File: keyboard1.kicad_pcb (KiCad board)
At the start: 2 copper layers, 117.5 x 78.5 mm, 46 parts, among them SW1 SW_PUSH, SW10 SW_PUSH, SW11 SW_PUSH, SW12 SW_PUSH, SW13 SW_PUSH, SW14 SW_PUSH, SW15 SW_PUSH, SW16 SW_PUSH, SW17 SW_PUSH, SW18 SW_PUSH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

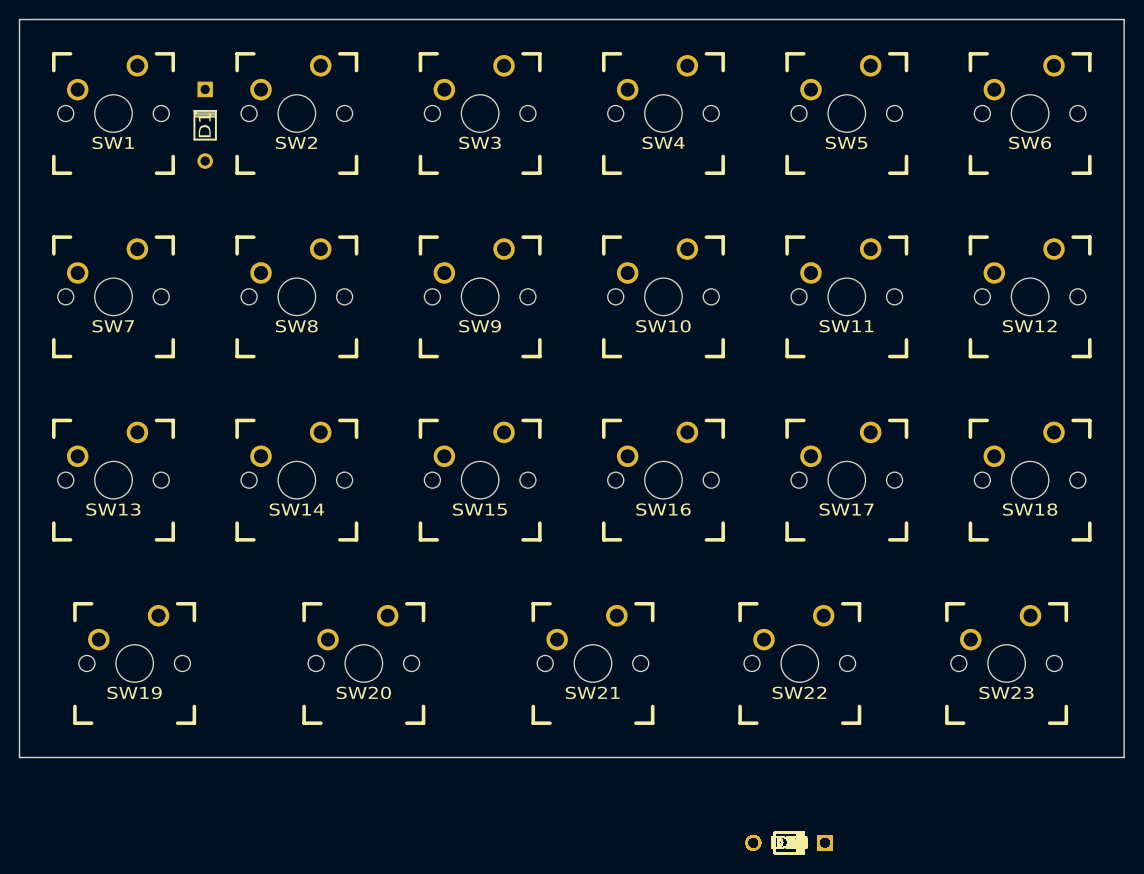
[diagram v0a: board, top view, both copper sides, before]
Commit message: Basic schematic complete, routing in progress
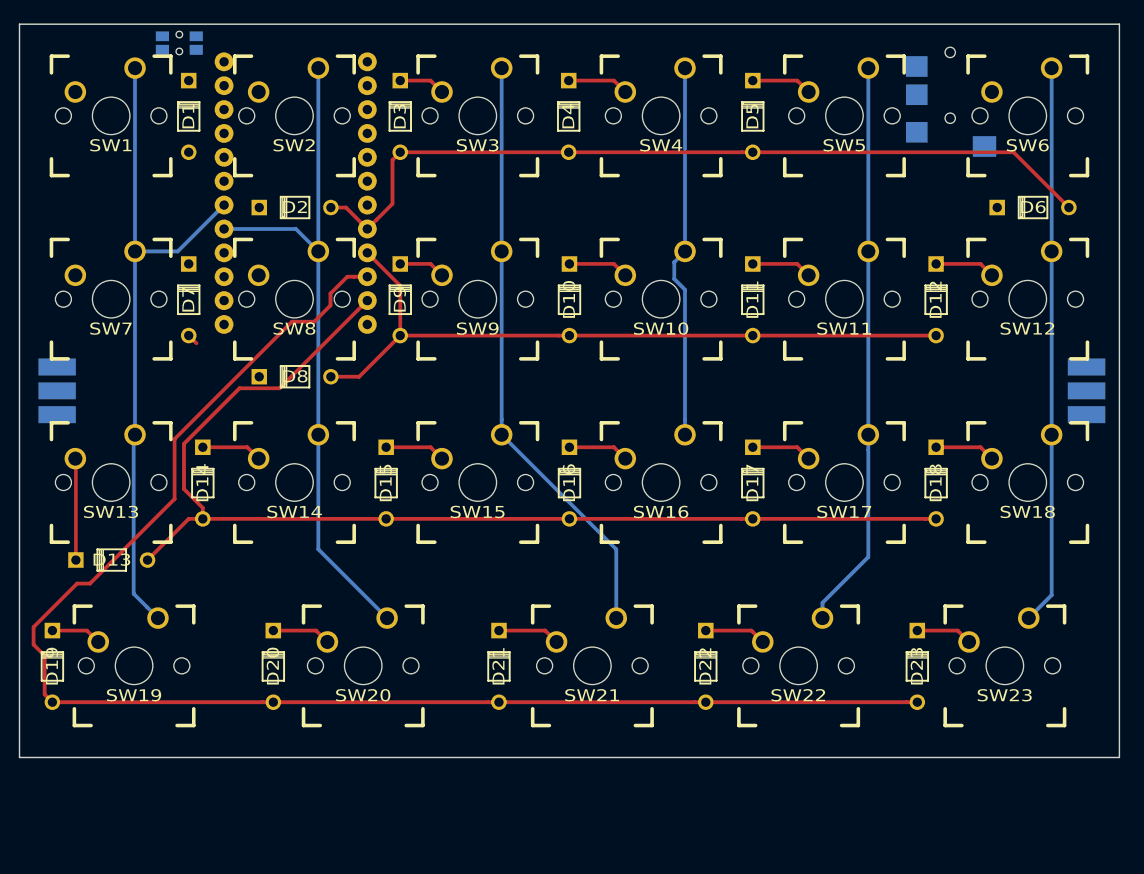
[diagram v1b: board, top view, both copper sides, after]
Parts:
- added J1: CONN_01X03, lib_fp:WS2812_3PIN, B.Cu at (94.0, 101.0)
- added J2: CONN_01X03, lib_fp:WS2812_3PIN, B.Cu at (203.5, 101.0)
- added J3: SJ2-3574A-SMT, lib_fp:SJ2-3574A-SMT, B.Cu at (189.0, 68.5)
- added SW24: SW_PUSH, Buttons_Switches_SMD:SW_SPST_EVQP7C, B.Cu at (107.0, 64.0)
- added U1: arduino_pro_micro, lib_fp:arduino-pro-micro, B.Cu at (127.0, 66.0)
- SW1, SW10, SW11, SW12, SW13, SW14, SW15, SW16, SW17, SW18, SW2, SW22, SW3, SW4, SW5, SW6, SW7, SW8, SW9: footprint Keyboard:CHERRY_PCB_100H -> lib_fp:CHERRY_PCB_100H
- SW19, SW20, SW21, SW23: footprint Keyboard:CHERRY_PCB_125H -> lib_fp:CHERRY_PCB_125H
- moved D3 87.7 mm to (130.5, 71.8), turned to 90 degrees
- moved D7 86.1 mm to (108.0, 91.3), turned to 90 degrees
- moved D2 85.6 mm to (119.3, 81.5), turned to 180 degrees
- moved D4 80.8 mm to (148.4, 71.8), turned to 90 degrees
- moved D19 80.6 mm to (93.5, 130.3), turned to 90 degrees
- moved D13 78.1 mm to (99.8, 119.0), turned to 180 degrees
- moved D5 77.4 mm to (168.0, 71.8), turned to 90 degrees
- moved D14 73.2 mm to (109.5, 110.8), turned to 90 degrees
- moved D6 72.4 mm to (197.8, 81.5), turned to 180 degrees
- moved D8 72.3 mm to (119.3, 99.5), turned to 180 degrees
- moved D9 71.1 mm to (130.5, 91.3), turned to 90 degrees
- moved D10 62.3 mm to (148.5, 91.3), turned to 90 degrees
- moved D12 59.8 mm to (187.5, 91.3), turned to 90 degrees
- moved D20 58.0 mm to (117.0, 130.3), turned to 90 degrees
- moved D11 57.9 mm to (168.0, 91.3), turned to 90 degrees
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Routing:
- net ROW4: track 0.00 -> 156.2 mm
- net ROW3: track 0.00 -> 120.3 mm
- net ROW1: track 0.00 -> 88.0 mm
- net ROW2: track 0.00 -> 77.6 mm
- net COL2: track 0.00 -> 72.5 mm
- net COL1: track 0.00 -> 71.1 mm
- net COL3: track 0.00 -> 63.5 mm
- net COL5: track 0.00 -> 60.5 mm
- net COL6: track 0.00 -> 59.5 mm
- net COL4: track 0.00 -> 39.9 mm
- net Net-(D13-Pad2): track 0.00 -> 10.8 mm
- net Net-(D4-Pad2): track 0.00 -> 7.60 mm
- net Net-(D21-Pad2): track 0.00 -> 6.63 mm
- net Net-(D22-Pad2): track 0.00 -> 6.57 mm
- net Net-(D14-Pad2): track 0.00 -> 6.44 mm
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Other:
- board size 117.5 x 78.5 mm -> 117 x 78 mm
